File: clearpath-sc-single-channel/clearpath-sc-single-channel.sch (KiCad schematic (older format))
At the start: 53 parts, among them P1 MOLEX_MICROFIT_JR_RH_2x1_WAY, P2 MOLEX_MICROFIT_JR_RH_2x2_WAY, P3 MOLEX_MICROFIT_JR_RH_2x2_WAY, P4 MOLEX_MICROFIT_JR_RH_2x4_WAY, Q1 MMBT5401, Q2 MMBTA06, U1 LM317LCPK, U2 FT230XS-R, U3 USBLC6, U4 LM317LCPK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

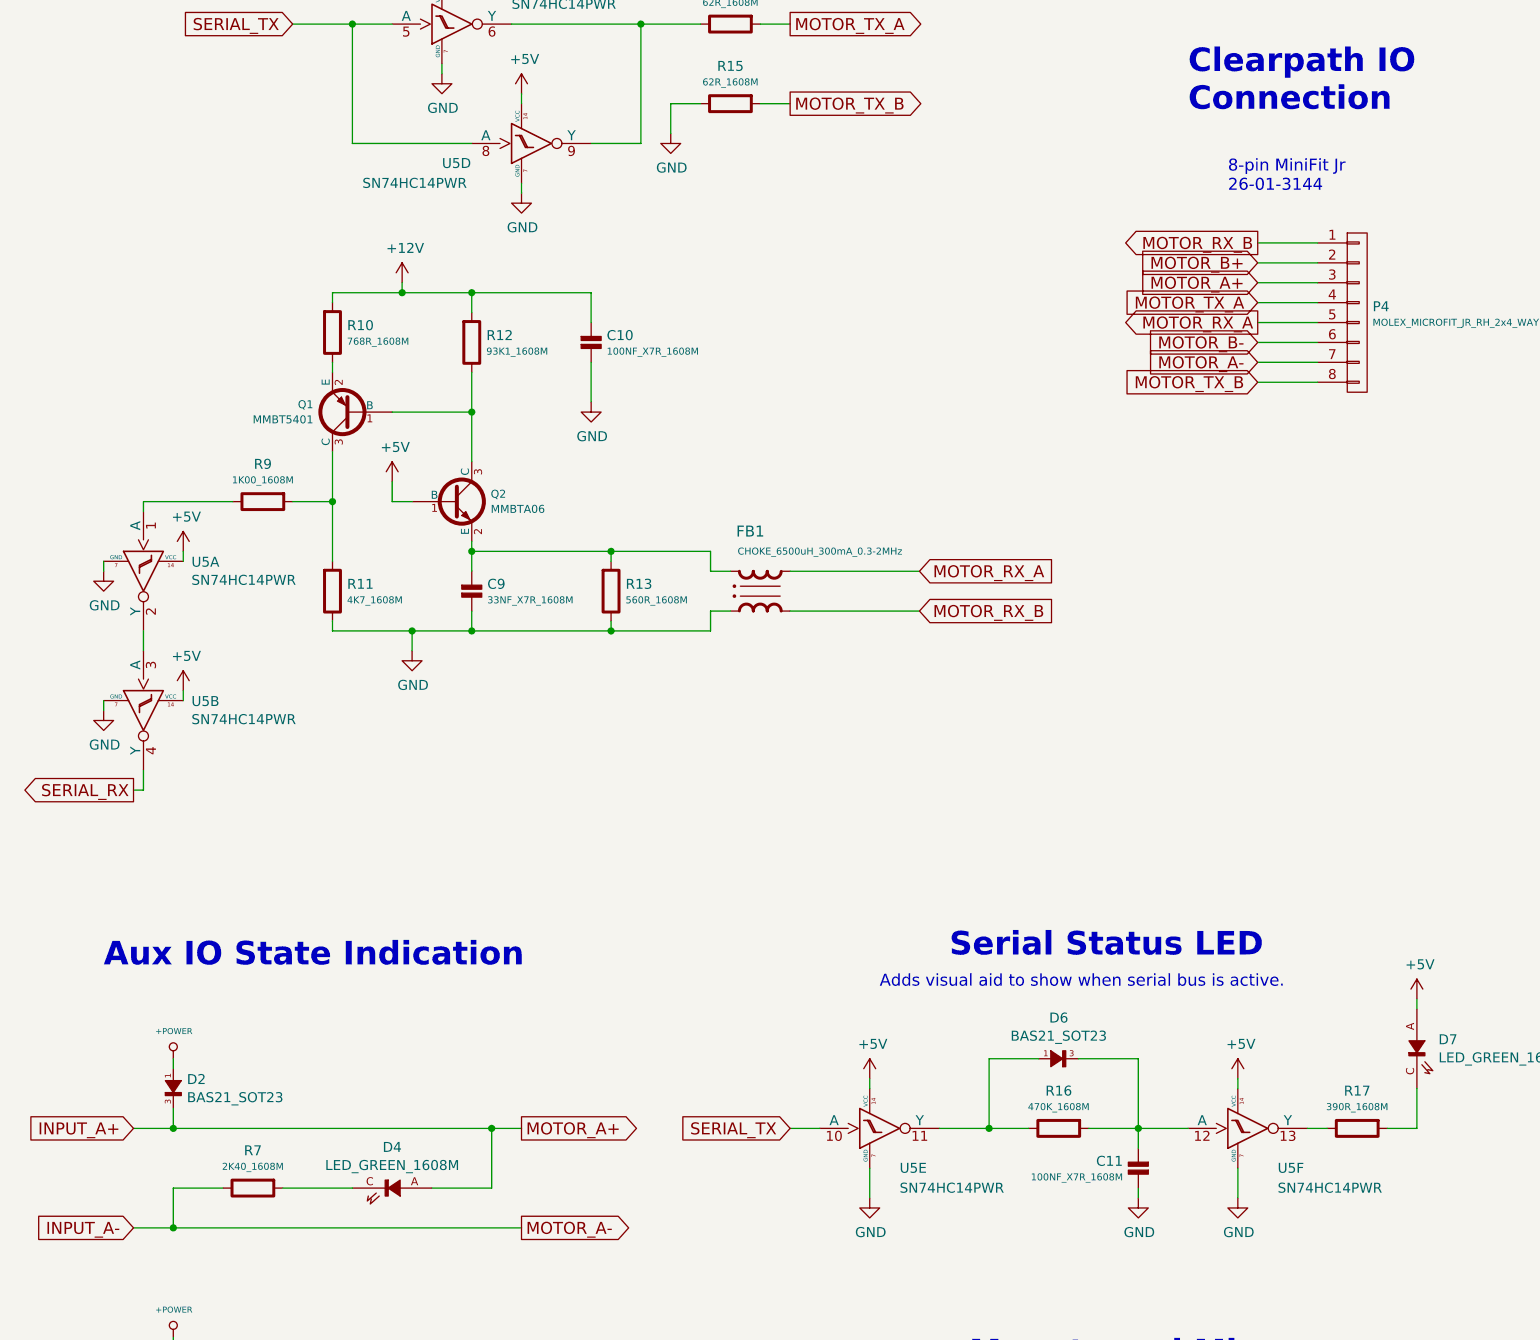
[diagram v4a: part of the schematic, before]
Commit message: Reworked hex inverter and finished routing
Increased trace thickness, all drc errors removed, improved hex schmitt wiring by shuffling unit allocation in schematic.
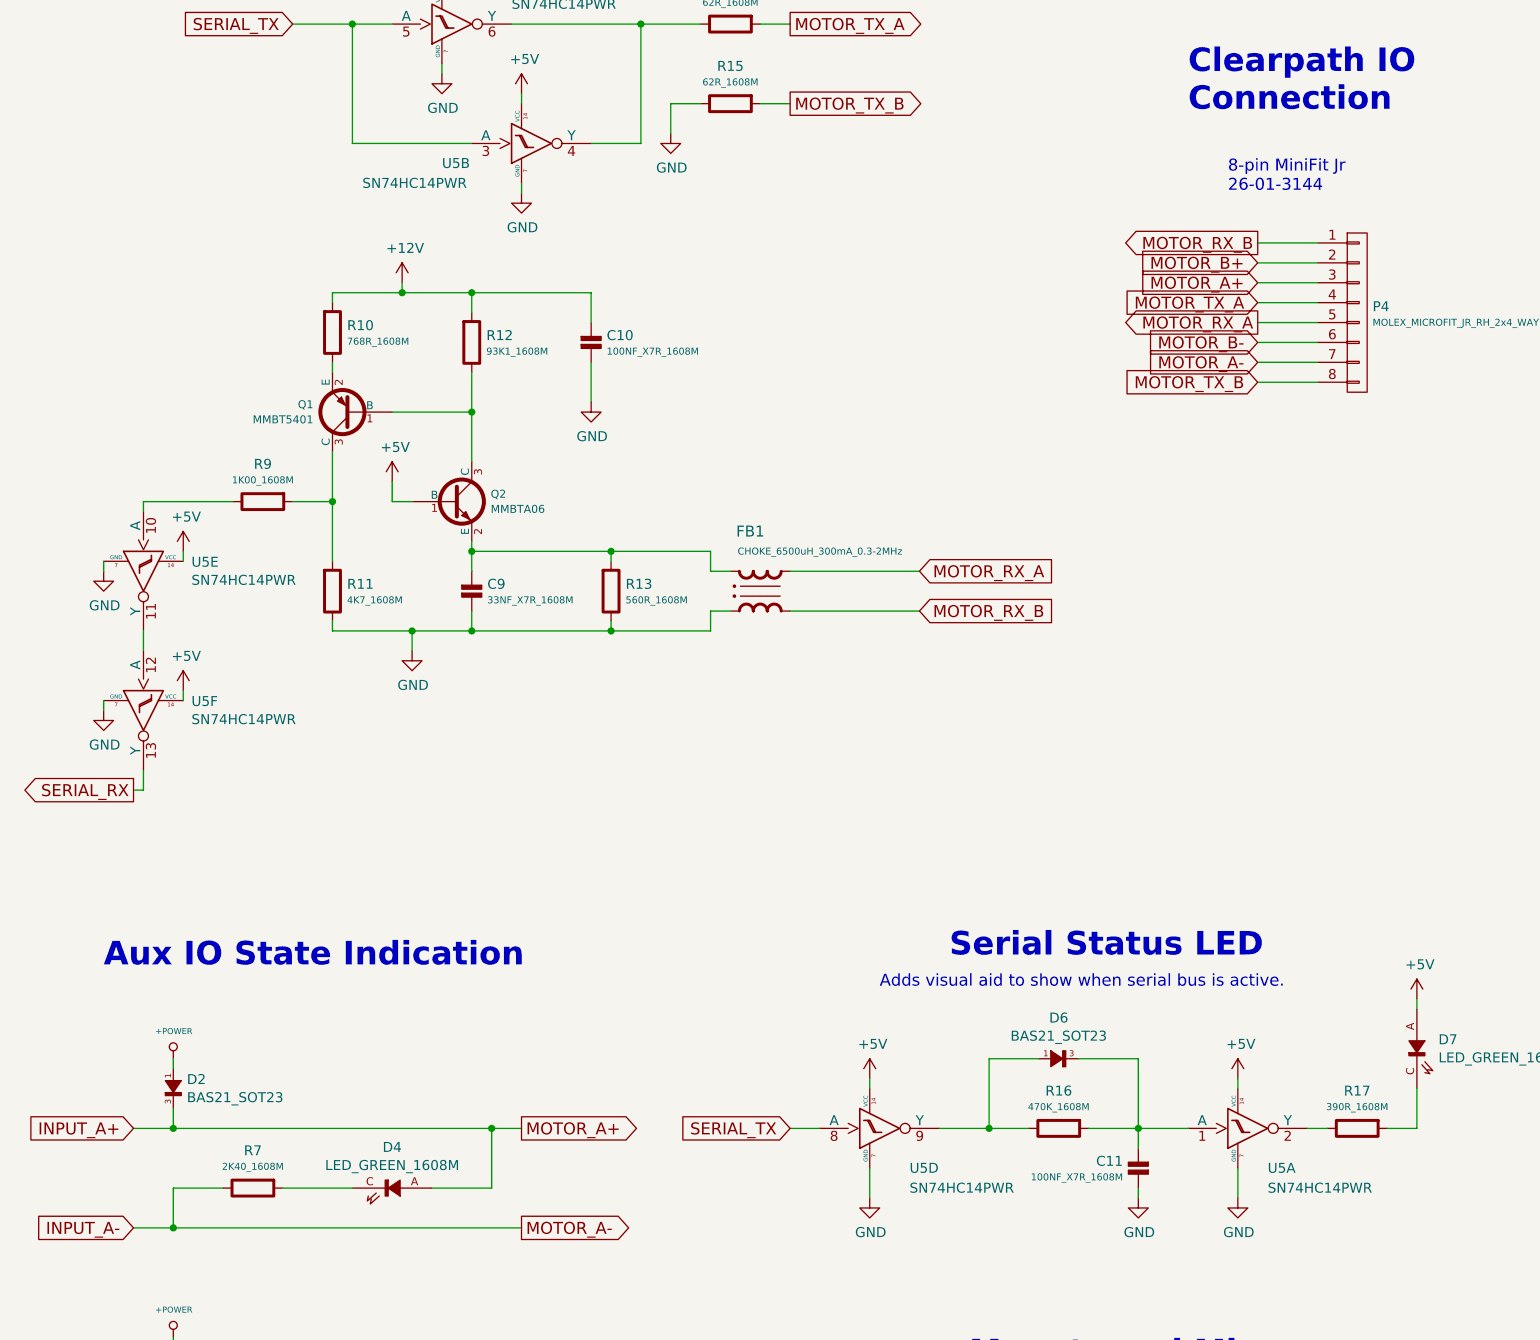
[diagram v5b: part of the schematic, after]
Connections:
- net SERIAL_RX: now also U5.13 (Y); no longer U5.4 (Y)
- net SERIAL_TX: now also U5.3 (A), U5.8 (A); no longer U5.10 (A), U5.8 (A)
- net at R9.2: now also U5.10 (A); no longer U5.1 (A)
- net at R14.2, U5.6 (Y): now also U5.4 (Y); no longer U5.9 (Y)
- net at R17.2: now also U5.2 (Y); no longer U5.13 (Y)
- net at C11.1, D6.3 (C), R16.1: now also U5.1 (A); no longer U5.12 (A)
- net at D6.1 (A), R16.2: now also U5.9 (Y); no longer U5.11 (Y)
- new net: U5.11 (Y), U5.12 (A)
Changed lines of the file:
@@
 $Comp
 L SN74HC14PWR U5
-U 4 1 59C88EF8
+U 2 1 59C88EF8
 P 10500 2600
 F 0 "U5" H 10100 2500 50  0000 L CNN
@@
 F 9 "0.456" H 10500 2040 20  0001 C CNN "Supplier Price"
 F 10 "10" H 10500 2015 20  0001 C CNN "Supplier Price Break"
-	4    10500 2600
+	2    10500 2600
 	1    0    0    -1
 $EndComp
@@
 $Comp
 L SN74HC14PWR U5
-U 1 1 59C8ACB0
+U 5 1 59C8ACB0
 P 8600 4700
 F 0 "U5" V 8604 4941 50  0000 L CNN
@@
 F 9 "0.456" H 8600 4140 20  0001 C CNN "Supplier Price"
 F 10 "10" H 8600 4115 20  0001 C CNN "Supplier Price Break"
-	1    8600 4700
+	5    8600 4700
 	0    1    1    0
 $EndComp
 $Comp
 L SN74HC14PWR U5
-U 2 1 59C8ADBA
+U 6 1 59C8ADBA
 P 8600 5400
 F 0 "U5" V 8604 5641 50  0000 L CNN
@@
 F 9 "0.456" H 8600 4840 20  0001 C CNN "Supplier Price"
 F 10 "10" H 8600 4815 20  0001 C CNN "Supplier Price Break"
-	2    8600 5400
+	6    8600 5400
 	0    1    1    0
 $EndComp
 $Comp
 L SN74HC14PWR U5
-U 5 1 59C8AF5F
+U 1 1 59C8AF5F
+P 14100 7550
+F 0 "U5" H 14250 7350 50  0000 L CNN
+F 1 "SN74HC14PWR" H 14250 7250 50  0000 L CNN
+F 2 "Applidyne_SOP:SOP14P65_500X640X120L62X24N" H 14100 7190 20  0001 C CNN
+F 3 "http://www.ti.com/lit/gpn/sn74hc14" H 14100 7165 20  0001 C CNN
+F 4 "TI" H 14100 7115 20  0001 C CNN "manf"
+F 5 "SN74HC14PWR" H 14100 7090 20  0001 C CNN "manf#"
+F 6 "Mouser" H 14100 7065 20  0001 C CNN "Supplier"
+F 7 "595-SN74HC14PWR" H 14100 7040 20  0001 C CNN "Supplier Part No"
+F 8 "http://au.mouser.com/ProductDetail/Texas-Instruments/SN74HC14PWR/?qs=sGAEpiMZZMutVWjHE%2fYQw9XSWsf7N%2fuyBxLji%2fG2WzM%3d" H 14100 7015 20  0001 C CNN "Supplier URL"
+F 9 "0.456" H 14100 6990 20  0001 C CNN "Supplier Price"
+F 10 "10" H 14100 6965 20  0001 C CNN "Supplier Price Break"
+	1    14100 7550
+	1    0    0    -1
+$EndComp
+$Comp
+L SN74HC14PWR U5
+U 4 1 59C8B171
 P 12250 7550
-F 0 "U5" H 12400 7350 50  0000 L CNN
-F 1 "SN74HC14PWR" H 12400 7250 50  0000 L CNN
+F 0 "U5" H 12450 7350 50  0000 L CNN
+F 1 "SN74HC14PWR" H 12450 7250 50  0000 L CNN
 F 2 "Applidyne_SOP:SOP14P65_500X640X120L62X24N" H 12250 7190 20  0001 C CNN
 F 3 "http://www.ti.com/lit/gpn/sn74hc14" H 12250 7165 20  0001 C CNN
@@
 F 9 "0.456" H 12250 6990 20  0001 C CNN "Supplier Price"
 F 10 "10" H 12250 6965 20  0001 C CNN "Supplier Price Break"
-	5    12250 7550
+	4    12250 7550
 	1    0    0    -1
 $EndComp
-$Comp
-L SN74HC14PWR U5
-U 6 1 59C8B171
-P 14100 7550
-F 0 "U5" H 14300 7350 50  0000 L CNN
-F 1 "SN74HC14PWR" H 14300 7250 50  0000 L CNN
-F 2 "Applidyne_SOP:SOP14P65_500X640X120L62X24N" H 14100 7190 20  0001 C CNN
-F 3 "http://www.ti.com/lit/gpn/sn74hc14" H 14100 7165 20  0001 C CNN
-F 4 "TI" H 14100 7115 20  0001 C CNN "manf"
-F 5 "SN74HC14PWR" H 14100 7090 20  0001 C CNN "manf#"
-F 6 "Mouser" H 14100 7065 20  0001 C CNN "Supplier"
-F 7 "595-SN74HC14PWR" H 14100 7040 20  0001 C CNN "Supplier Part No"
-F 8 "http://au.mouser.com/ProductDetail/Texas-Instruments/SN74HC14PWR/?qs=sGAEpiMZZMutVWjHE%2fYQw9XSWsf7N%2fuyBxLji%2fG2WzM%3d" H 14100 7015 20  0001 C CNN "Supplier URL"
-F 9 "0.456" H 14100 6990 20  0001 C CNN "Supplier Price"
-F 10 "10" H 14100 6965 20  0001 C CNN "Supplier Price Break"
-	6    14100 7550
-	1    0    0    -1
-$EndComp

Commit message: Cosmetic improvements
Added silkscreen text and voltage test points
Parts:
- added TEST1, TEST2: CLIP_HOOK_RED, Applidyne_Test:KEYSTONE_5000, symbol CLIP_HOOK_RED
- added TEST3: CLIP_HOOK_BLACK, Applidyne_Test:KEYSTONE_5001, symbol CLIP_HOOK_BLACK
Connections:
- net +12V: now also TEST1.1 (PAD)
- net +5V: now also TEST2.1 (PAD)
- net GND: now also TEST3.1 (PAD)
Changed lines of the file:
@@
 LIBS:appli_connector_molex
 LIBS:appli_connector_jst
+LIBS:appli_connector_wurth
 LIBS:appli_crystal
 LIBS:appli_device
@@
 Connection ~ 2250 3600
 Wire Wire Line
-	2700 3600 2800 3600
-Wire Wire Line
-	2800 3600 2800 3150
+	2800 3600 2700 3600
+Wire Wire Line
+	2800 3050 2800 3600
 Connection ~ 2800 3150
 Wire Wire Line
@@
 Connection ~ 4950 3600
 Wire Wire Line
-	5400 3600 5500 3600
-Wire Wire Line
-	5500 3600 5500 3150
+	5500 3600 5400 3600
+Wire Wire Line
+	5500 3050 5500 3600
 Connection ~ 5500 3150
 Wire Wire Line
@@
 	-1   0    0    -1
 $EndComp
+$Comp
+L CLIP_HOOK_RED TEST2
+U 1 1 59CC6BA9
+P 5500 3050
+F 0 "TEST2" V 5431 3228 39  0000 L CNN
+F 1 "CLIP_HOOK_RED" H 5550 3050 39  0001 L TNN
+F 2 "Applidyne_Test:KEYSTONE_5000" H 5550 3000 39  0001 L TNN
+F 3 "http://www.farnell.com/datasheets/1703983.pdf" H 5550 2850 39  0001 L BNN
+F 4 "KEYSTONE" H 5550 2950 39  0001 L TNN "manf"
+F 5 "5000" H 5550 2800 39  0001 L BNN "manf#"
+F 6 "Element14" H 5550 2750 39  0001 L BNN "Supplier"
+F 7 "1463076" H 5550 2700 39  0001 L BNN "Supplier Part No"
+F 8 "http://au.element14.com/keystone/5000/test-point-pcb-through-hole/dp/1463076" H 5550 2650 39  0001 L BNN "Supplier URL"
+F 9 "0.23" H 5550 2600 39  0001 L BNN "Supplier Price"
+F 10 "100" H 5550 2550 39  0001 L BNN "Suppier Price Break"
+	1    5500 3050
+	0    1    1    0
+$EndComp
+$Comp
+L CLIP_HOOK_RED TEST1
+U 1 1 59CC7BF6
+P 2800 3050
+F 0 "TEST1" V 2731 3228 39  0000 L CNN
+F 1 "CLIP_HOOK_RED" H 2850 3050 39  0001 L TNN
+F 2 "Applidyne_Test:KEYSTONE_5000" H 2850 3000 39  0001 L TNN
+F 3 "http://www.farnell.com/datasheets/1703983.pdf" H 2850 2850 39  0001 L BNN
+F 4 "KEYSTONE" H 2850 2950 39  0001 L TNN "manf"
+F 5 "5000" H 2850 2800 39  0001 L BNN "manf#"
+F 6 "Element14" H 2850 2750 39  0001 L BNN "Supplier"
+F 7 "1463076" H 2850 2700 39  0001 L BNN "Supplier Part No"
+F 8 "http://au.element14.com/keystone/5000/test-point-pcb-through-hole/dp/1463076" H 2850 2650 39  0001 L BNN "Supplier URL"
+F 9 "0.23" H 2850 2600 39  0001 L BNN "Supplier Price"
+F 10 "100" H 2850 2550 39  0001 L BNN "Suppier Price Break"
+	1    2800 3050
+	0    1    1    0
+$EndComp
+$Comp
+L CLIP_HOOK_BLACK TEST3
+U 1 1 59CC9035
+P 6450 3150
+F 0 "TEST3" V 6381 3328 39  0000 L CNN
+F 1 "CLIP_HOOK_BLACK" H 6500 3150 39  0001 L TNN
+F 2 "Applidyne_Test:KEYSTONE_5001" H 6500 3100 39  0001 L TNN
+F 3 "http://www.farnell.com/datasheets/1703983.pdf" H 6500 2950 39  0001 L BNN
+F 4 "KEYSTONE" H 6500 3050 39  0001 L TNN "manf"
+F 5 "5001" H 6500 2900 39  0001 L BNN "manf#"
+F 6 "Element14" H 6500 2850 39  0001 L BNN "Supplier"
+F 7 "2301278" H 6500 2800 39  0001 L BNN "Supplier Part No"
+F 8 "http://au.element14.com/keystone/5001/test-point-pcb-through-hole/dp/2301278" H 6500 2750 39  0001 L BNN "Supplier URL"
+F 9 "0.218" H 6500 2700 39  0001 L BNN "Supplier Price"
+F 10 "100" H 6500 2650 39  0001 L BNN "Suppier Price Break"
+	1    6450 3150
+	0    1    1    0
+$EndComp
+Wire Wire Line
+	6450 3150 6450 3700
+$Comp
+L GND #PWR048
+U 1 1 59CC9E4F
+P 6450 3700
+F 0 "#PWR048" H 6450 3450 50  0001 C CNN
+F 1 "GND" H 6455 3527 50  0000 C CNN
+F 2 "" H 6450 3700 60  0000 C CNN
+F 3 "" H 6450 3700 60  0000 C CNN
+	1    6450 3700
+	1    0    0    -1
+$EndComp
 $EndSCHEMATC
